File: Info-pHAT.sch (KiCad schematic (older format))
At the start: 17 parts, among them SW1 SW_DIP_x01, SW2 SW_DIP_x01, SW3 SW_DIP_x01, U1 CAT24C32WI-GT3

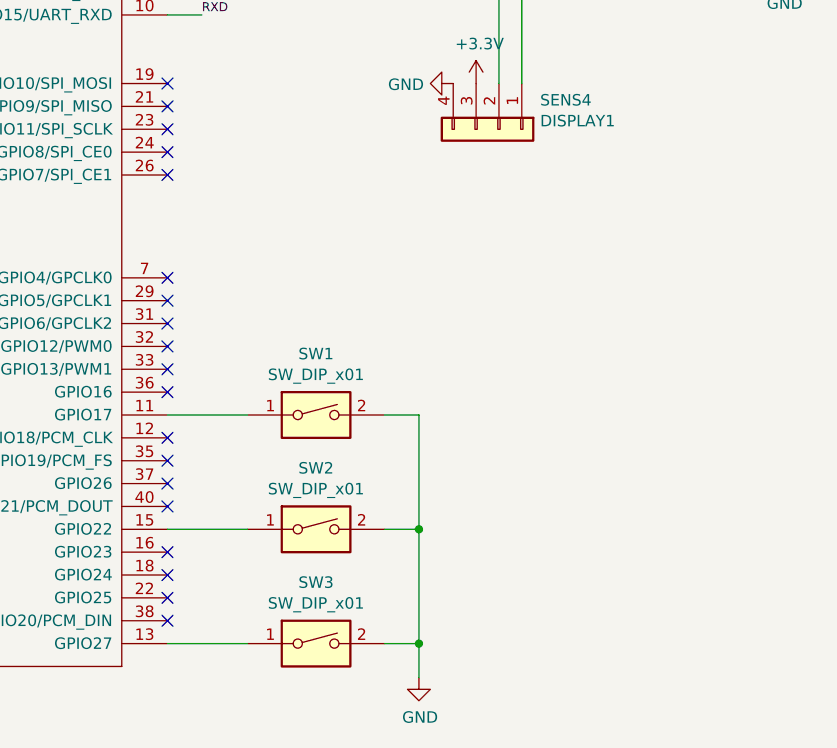
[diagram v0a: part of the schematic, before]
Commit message: Info-pHAT.pro: Add LED D1 and D2
Add indication LEDs D1 and D2.

Signed-off-by: Leon Anavi <leon@anavi.org>
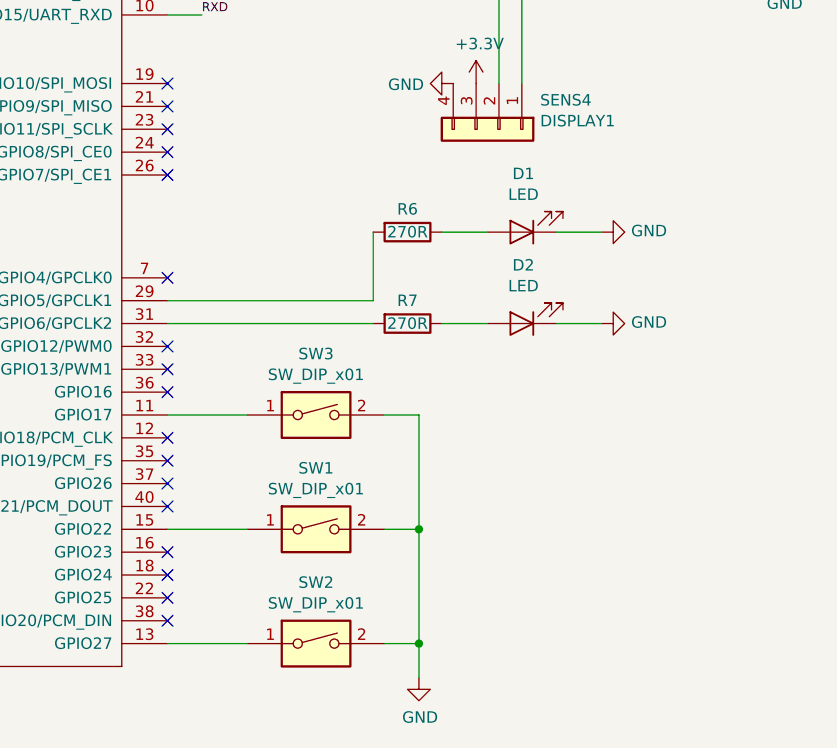
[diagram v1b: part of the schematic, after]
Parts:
- added D1, D2: LED, LED_SMD:LED_1206_3216Metric, symbol Device:LED
- added R6, R7: 270R, Resistors_SMD:R_0603_HandSoldering, symbol Device:R
- renumbered SW2 to SW1, SW3 to SW2, SW1 to SW3
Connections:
- net GND: now also D1.1 (K), D2.1 (K)
- net at RASP_CONN1.29 (GPIO5/GPCLK1): now also R6.2
- net at RASP_CONN1.31 (GPIO6/GPCLK2): now also R7.2
- new net: D2.2 (A), R7.1
- new net: D1.2 (A), R6.1
- no-connect marks 19 -> 17
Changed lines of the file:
@@
 EESchema Schematic File Version 4
-LIBS:Info-pHAT-cache
-EELAYER 26 0
+EELAYER 30 0
 EELAYER END
 $Descr A4 11693 8268
@@
 NoConn ~ 5350 4350
 NoConn ~ 5350 4250
-NoConn ~ 5350 3550
-NoConn ~ 5350 3650
 NoConn ~ 5350 3750
 NoConn ~ 5350 3850
@@
 	6900 2100 6900 2600
 $Comp
-L Switch:SW_DIP_x01 SW1
+L Switch:SW_DIP_x01 SW3
 U 1 1 5E29052A
 P 6000 4050
-F 0 "SW1" H 6000 4317 50  0000 C CNN
+F 0 "SW3" H 6000 4317 50  0000 C CNN
 F 1 "SW_DIP_x01" H 6000 4226 50  0000 C CNN
 F 2 "Buttons_Switches_ThroughHole:SW_PUSH_6mm_h4.3mm" H 6000 4050 50  0001 C CNN
@@
 $EndComp
 $Comp
-L Switch:SW_DIP_x01 SW2
+L Switch:SW_DIP_x01 SW1
 U 1 1 5E290640
 P 6000 4550
-F 0 "SW2" H 6000 4817 50  0000 C CNN
+F 0 "SW1" H 6000 4817 50  0000 C CNN
 F 1 "SW_DIP_x01" H 6000 4726 50  0000 C CNN
 F 2 "Buttons_Switches_ThroughHole:SW_PUSH_6mm_h4.3mm" H 6000 4550 50  0001 C CNN
@@
 $EndComp
 $Comp
-L Switch:SW_DIP_x01 SW3
+L Switch:SW_DIP_x01 SW2
 U 1 1 5E2907C7
 P 6000 5050
-F 0 "SW3" H 6000 5317 50  0000 C CNN
+F 0 "SW2" H 6000 5317 50  0000 C CNN
 F 1 "SW_DIP_x01" H 6000 5226 50  0000 C CNN
 F 2 "Buttons_Switches_ThroughHole:SW_PUSH_6mm_h4.3mm" H 6000 5050 50  0001 C CNN
@@
 	6450 4050 6450 4550
 Connection ~ 6450 4550
+$Comp
+L Device:R R7
+U 1 1 60D2B963
+P 6400 3650
+F 0 "R7" V 6300 3650 50  0000 C CNN
+F 1 "270R" V 6400 3650 50  0000 C CNN
+F 2 "Resistors_SMD:R_0603_HandSoldering" V 6330 3650 50  0001 C CNN
+F 3 "~" H 6400 3650 50  0001 C CNN
+	1    6400 3650
+	0    1    1    0
+$EndComp
+$Comp
+L Device:R R6
+U 1 1 60D2C5C4
+P 6400 3250
+F 0 "R6" V 6300 3250 50  0000 C CNN
+F 1 "270R" V 6400 3250 50  0000 C CNN
+F 2 "Resistors_SMD:R_0603_HandSoldering" V 6330 3250 50  0001 C CNN
+F 3 "~" H 6400 3250 50  0001 C CNN
+	1    6400 3250
+	0    1    1    0
+$EndComp
+Wire Wire Line
+	5350 3650 6250 3650
+Wire Wire Line
+	5350 3550 6250 3550
+Wire Wire Line
+	6250 3550 6250 3250
+$Comp
+L Device:LED D1
+U 1 1 60D32733
+P 6900 3250
+F 0 "D1" H 6893 2995 50  0000 C CNN
+F 1 "LED" H 6893 3086 50  0000 C CNN
+F 2 "LED_SMD:LED_1206_3216Metric" H 6900 3250 50  0001 C CNN
+F 3 "~" H 6900 3250 50  0001 C CNN
+	1    6900 3250
+	-1   0    0    1
+$EndComp
+$Comp
+L Device:LED D2
+U 1 1 60D32D35
+P 6900 3650
+F 0 "D2" H 6893 3395 50  0000 C CNN
+F 1 "LED" H 6893 3486 50  0000 C CNN
+F 2 "LED_SMD:LED_1206_3216Metric" H 6900 3650 50  0001 C CNN
+F 3 "~" H 6900 3650 50  0001 C CNN
+	1    6900 3650
+	-1   0    0    1
+$EndComp
+$Comp
+L Info-pHAT-rescue:GND #PWR0104
+U 1 1 60D3357A
+P 7250 3250
+F 0 "#PWR0104" H 7250 3000 50  0001 C CNN
+F 1 "GND" V 7255 3122 50  0000 R CNN
+F 2 "" H 7250 3250 50  0000 C CNN
+F 3 "" H 7250 3250 50  0000 C CNN
+	1    7250 3250
+	0    -1   -1   0
+$EndComp
+$Comp
+L Info-pHAT-rescue:GND #PWR0105
+U 1 1 60D33C1E
+P 7250 3650
+F 0 "#PWR0105" H 7250 3400 50  0001 C CNN
+F 1 "GND" V 7255 3522 50  0000 R CNN
+F 2 "" H 7250 3650 50  0000 C CNN
+F 3 "" H 7250 3650 50  0000 C CNN
+	1    7250 3650
+	0    -1   -1   0
+$EndComp
+Wire Wire Line
+	7050 3250 7250 3250
+Wire Wire Line
+	7050 3650 7250 3650
+Wire Wire Line
+	6550 3650 6750 3650
+Wire Wire Line
+	6550 3250 6750 3250
 $EndSCHEMATC
